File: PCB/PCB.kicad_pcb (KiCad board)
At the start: 2 copper layers, 15 parts, among them J1 Conn_01x04_Pin, J2 Conn_01x04_Pin, J3 Conn_01x04_Pin, SW1 SW_SPDT, SW2 SW_Push, U1 ESP32-DevKitC

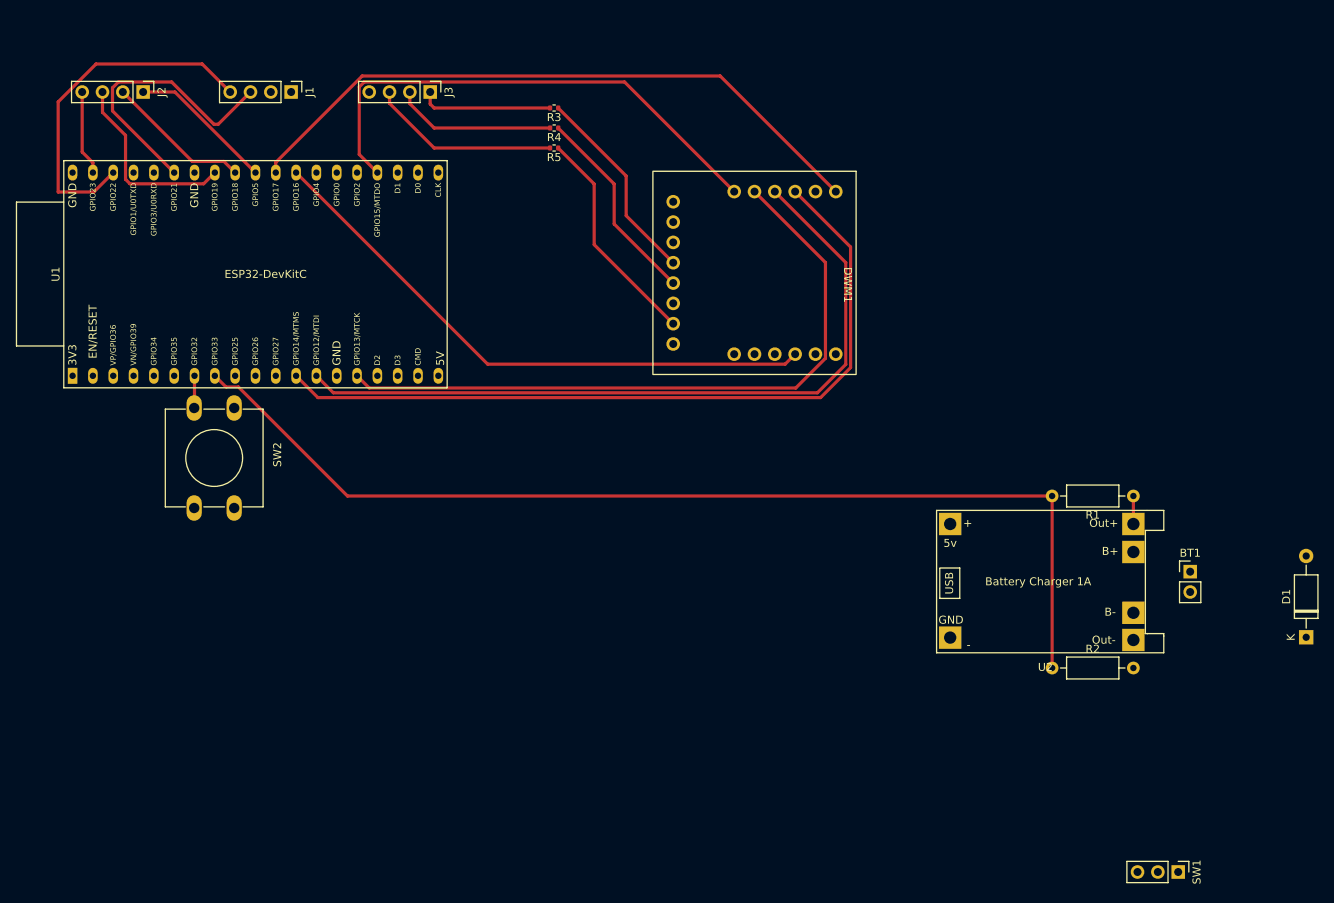
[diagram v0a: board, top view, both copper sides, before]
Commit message: PCB is finished, but esp is the wrong way :(
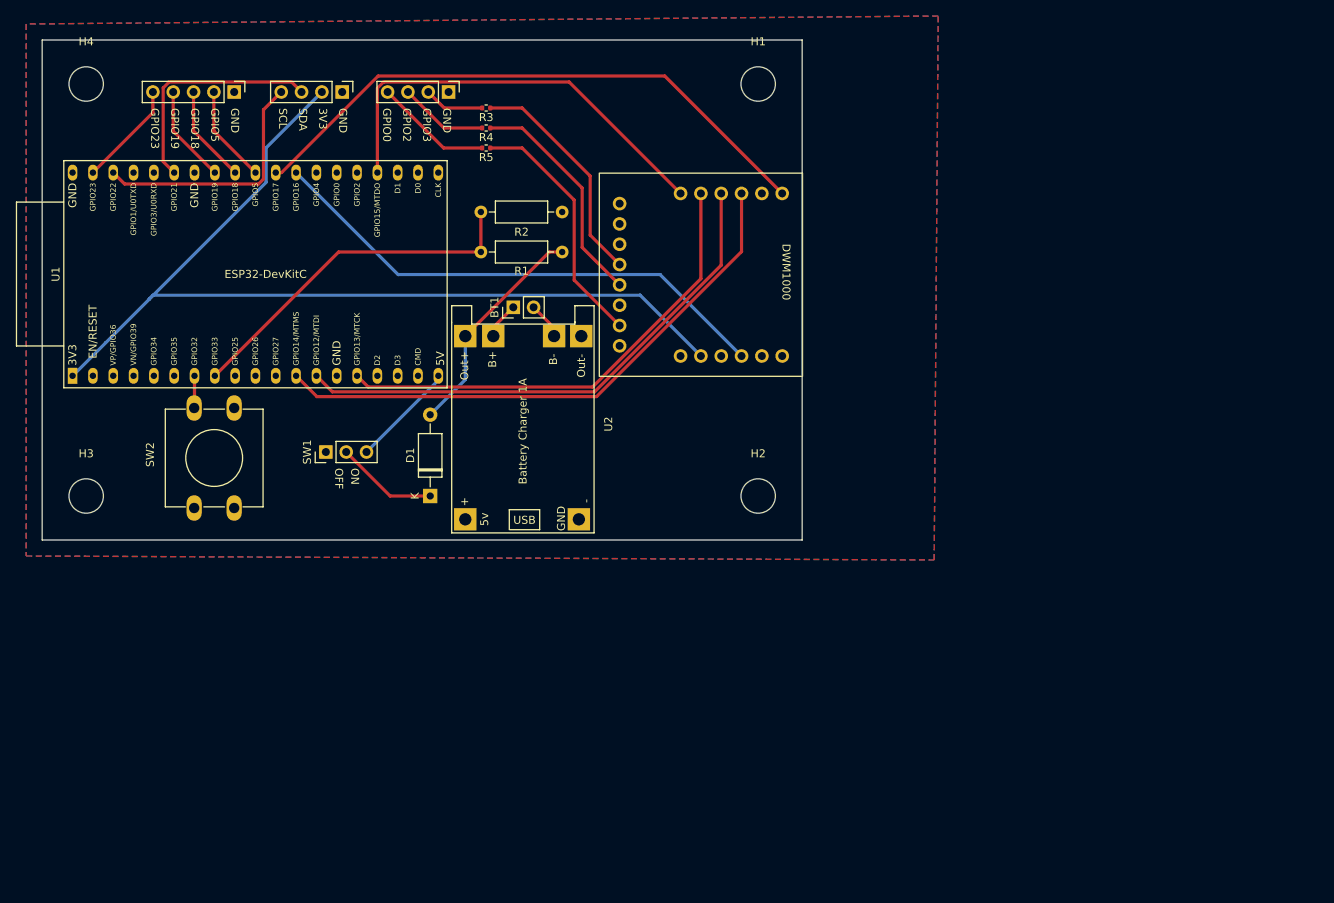
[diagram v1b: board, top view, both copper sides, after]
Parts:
- added H1: MountingHole, MountingHole:MountingHole_4.3mm_M4, F.Cu at (134.0, 57.5)
- added H2: MountingHole, MountingHole:MountingHole_4.3mm_M4, F.Cu at (134.0, 109.0)
- added H3: MountingHole, MountingHole:MountingHole_4.3mm_M4, F.Cu at (50.0, 109.0)
- added H4: MountingHole, MountingHole:MountingHole_4.3mm_M4, F.Cu at (50.0, 57.5)
- J2: value Conn_01x04_Pin -> Conn_01x05_Pin; footprint Connector_PinHeader_2.54mm:PinHeader_1x04_P2.54mm_Vertical -> Connector_PinHeader_2.54mm:PinHeader_1x05_P2.54mm_Vertical
- moved SW1 118.8 mm to (80.0, 103.5), turned to 90 degrees
- moved D1 110.9 mm to (93.0, 109.0)
- moved R2 91.4 mm to (99.3, 73.5)
- moved BT1 90.8 mm to (103.4, 85.4), turned to 90 degrees
- moved R1 77.6 mm to (109.5, 78.5)
- moved U2 60.7 mm to (95.7, 113.6), turned to 90 degrees
- moved J2 11.4 mm to (68.5, 58.5)
- moved R4 8.50 mm to (100.0, 63.0)
- moved R3 8.49 mm to (100.0, 60.5)
- moved R5 8.49 mm to (100.0, 65.5)
- moved DWM1000 6.70 mm to (137.0, 81.3)
- moved J1 6.38 mm to (82.0, 58.5)
- moved J3 2.30 mm to (95.3, 58.5)
- renumbered DWM1 to DWM1000
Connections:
- J2 pad 1: /GPIO5 -> GND
- J2 pad 2: /GPIO18 -> /GPIO5
- J2 pad 3: /GPIO19 -> /GPIO18
- J2 pad 4: /GPIO23 -> /GPIO19
- J3 pad 1: Net-(J3-Pin_1) -> GND
- J3 pad 4: GND -> Net-(J3-Pin_4)
- R3 pad 2: Net-(J3-Pin_1) -> Net-(J3-Pin_2)
- R4 pad 2: Net-(J3-Pin_2) -> Net-(J3-Pin_3)
- R5 pad 2: Net-(J3-Pin_3) -> Net-(J3-Pin_4)
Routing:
- net +3.3V: track 0.00 -> 120.7 mm
- net VBAT: track 132.4 -> 44.7 mm
- net /MISO: track 93.8 -> 67.0 mm
- net /MOSI: track 85.2 -> 59.8 mm
- net /CLK: track 96.9 -> 71.5 mm
- net Net-(D1-A): track 3.50 -> 28.1 mm
- net Net-(J3-Pin_1): track 16.7 -> 0.00 mm
- net Net-(J3-Pin_4): track 0.00 -> 14.7 mm
- net Net-(SW1-C): track 0.00 -> 13.2 mm
- net +5V: track 0.00 -> 12.8 mm
- net Net-(J3-Pin_2): track 20.2 -> 7.56 mm
- net Net-(J3-Pin_3): track 23.8 -> 11.1 mm
- net /SCL: track 44.1 -> 31.4 mm
- net /GPIO19: track 24.1 -> 12.2 mm
- net /CS: track 64.4 -> 54.5 mm
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- added copper zone on B.Cu, net GND
- added copper zone on F.Cu, net GND
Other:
- board outline added: 95 x 62.5 mm
- board text added: "3V3"
- board text added: "GND"
- board text added: "GPIO0"
- board text added: "GPIO18"
- board text added: "GPIO19"
- board text added: "GPIO2"
- board text added: "GPIO23"
- board text added: "GPIO3"
- board text added: "GPIO5"
- board text added: "OFF"
- board text added: "ON"
- board text added: "SCL"
- board text added: "SDA"

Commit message: PCB redesign
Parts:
- H1, H2, H3, H4: footprint MountingHole:MountingHole_4.3mm_M4 -> MountingHole:MountingHole_3.2mm_M3
- moved H3 95.0 mm to (144.9, 113.7)
- moved H1 75.2 mm to (59.4, 67.2)
- moved J3 63.0 mm to (133.9, 108.2)
- moved U1 59.7 mm to (104.1, 72.8), turned to -90 degrees
- moved H4 57.0 mm to (59.4, 113.7)
- moved J1 52.5 mm to (65.1, 108.2), turned to 90 degrees
- moved J2 50.4 mm to (76.8, 108.2), turned to 90 degrees
- moved R3 50.2 mm to (131.4, 99.7), turned to -90 degrees
- moved R4 46.7 mm to (128.9, 99.7), turned to -90 degrees
- moved R5 43.2 mm to (126.4, 99.7), turned to -90 degrees
- moved H2 43.2 mm to (144.9, 67.2)
- moved D1 36.4 mm to (107.4, 75.5), turned to -90 degrees
- moved SW2 31.0 mm to (94.9, 114.2), turned to 90 degrees
- moved R2 22.7 mm to (121.9, 75.7), turned to -90 degrees
- moved SW1 17.3 mm to (65.3, 112.7)
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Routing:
- net Net-(U1-32K_XP/GPIO32/ADC1_CH4): track 4.04 -> 61.8 mm
- net +5V: track 12.8 -> 58.4 mm
- net /CS: track 54.5 -> 94.4 mm
- net Net-(SW1-C): track 13.2 -> 47.8 mm
- net /RST: track 65.2 -> 95.3 mm
- net +3.3V: track 120.7 -> 95.2 mm
- net Net-(DWM1000-GPIO0): track 31.2 -> 8.57 mm
- net /IRQ: track 74.4 -> 90.2 mm
- net Net-(DWM1000-GPIO2): track 28.6 -> 13.6 mm
- net Net-(D1-A): track 28.1 -> 14.6 mm
- net /MOSI: track 59.8 -> 72.6 mm
- net Net-(DWM1000-GPIO3): track 28.6 -> 17.2 mm
- net /GPIO23: track 13.2 -> 21.3 mm
- net Net-(J3-Pin_4): track 14.7 -> 8.02 mm
- net VBAT: track 44.7 -> 38.4 mm
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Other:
- board size 95 x 62.5 mm -> 94.5 x 55.5 mm
- board text added: "USB"
